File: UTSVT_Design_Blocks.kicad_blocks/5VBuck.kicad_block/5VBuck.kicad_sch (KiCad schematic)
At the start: 9 parts, among them U2 LMR51635XDDCR

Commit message: buck
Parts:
- removed C8: C_Small, symbol Device:C_Small
- C1: LCSC # C1607 -> (none); LCSC P/N (none) -> C1607; P/N (none) -> 581-0603YC225MAT2A
- C10, C9: footprint Capacitor_SMD:C_1210_3225Metric_Pad1.33x2.70mm_HandSolder -> Capacitor_SMD:C_0805_2012Metric_Pad1.18x1.45mm_HandSolder; LCSC P/N (none) -> C342635; P/N 81-GGM32ED70J476KE2L -> 581-TACR336K004X
- C2: footprint Capacitor_SMD:C_0603_1608Metric_Pad1.08x0.95mm_HandSolder -> Resistor_SMD:R_0201_0603Metric_Pad0.64x0.40mm_HandSolder; LCSC # C440198 -> (none); LCSC P/N (none) -> C14663
- L2: footprint Inductor_SMD:L_Sunlord_SWPA4020S -> Inductor_SMD:L_Cenker_CKCS252010; LCSC # C88247 -> (none); LCSC P/N (none) -> C354548; P/N (none) -> 810-VLS3015CX-100M-H
- R2: value 53.6 -> 53.6k; footprint Resistor_SMD:R_0603_1608Metric_Pad0.98x0.95mm_HandSolder -> Resistor_SMD:R_0201_0603Metric_Pad0.64x0.40mm_HandSolder; LCSC P/N (none) -> C23074; P/N 71-CRCW0603-53.6 -> 667-ERA-3ARB5362V; now fitted
- R3: footprint Capacitor_SMD:C_0402_1005Metric_Pad0.74x0.62mm_HandSolder -> Resistor_SMD:R_0201_0603Metric_Pad0.64x0.40mm_HandSolder; LCSC # C11660 -> (none); LCSC P/N (none) -> C22772; P/N (none) -> 603-RT0603DRE0710K2L; now fitted
- U2: LCSC P/N (none) -> C42432812; P/N (none) -> 595-LMR51635XDDCR
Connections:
- net V_in renamed V_in_24V
- net V_out renamed V_out_5V
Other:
- moved on the sheet: C10, C9, L2

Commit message: made changes
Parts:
- removed C10, C9: 33u, Capacitor_SMD:C_0805_2012Metric_Pad1.18x1.45mm_HandSolder, symbol Device:C_Small
- added C5, C8: 47u, Capacitor_SMD:C_1210_3225Metric_Pad1.33x2.70mm_HandSolder, symbol Device:C_Small
- C1: footprint Capacitor_SMD:C_0603_1608Metric_Pad1.08x0.95mm_HandSolder -> Capacitor_SMD:C_0805_2012Metric_Pad1.18x1.45mm_HandSolder; LCSC P/N C1607 -> C1771; P/N 581-0603YC225MAT2A -> 963-T21GCB7225MTPA1J
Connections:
- net GND: now also C5.2, C8.2
- net V_out_5V: now also C5.1, C8.1
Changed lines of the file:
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@@
 			)
 		)
-		(property "Footprint" "Capacitor_SMD:C_0603_1608Metric_Pad1.08x0.95mm_HandSolder"
+		(property "Footprint" "Capacitor_SMD:C_0805_2012Metric_Pad1.18x1.45mm_HandSolder"
 			(at 97.79 90.17 0)
 			(effects
@@
 			)
 		)
-		(property "LCSC P/N" "C1607"
+		(property "LCSC P/N" "C1771"
 			(at 97.79 90.17 0)
 			(effects
@@
 			)
 		)
-		(property "P/N" "581-0603YC225MAT2A"
+		(property "P/N" "963-T21GCB7225MTPA1J"
 			(at 97.79 90.17 0)
 			(effects
@@
 	)
 	(symbol
-		(lib_id "Device:C_Small")
-		(at 175.26 93.98 0)
-		(unit 1)
-		(exclude_from_sim no)
-		(in_bom yes)
-		(on_board yes)
-		(dnp no)
-		(fields_autoplaced yes)
-		(property "Reference" "C9"
-			(at 177.8 92.7162 0)
-			(effects
-				(font
-					(size 1.27 1.27)
-				)
-				(justify left)
-			)
-		)
-		(property "Value" "33u"
-			(at 177.8 95.2562 0)
-			(effects
-				(font
-					(size 1.27 1.27)
-				)
-				(justify left)
-			)
-		)
-		(property "Footprint" "Capacitor_SMD:C_0805_2012Metric_Pad1.18x1.45mm_HandSolder"
-			(at 175.26 93.98 0)
-			(effects
-				(font
-					(size 1.27 1.27)
-				)
-				(hide yes)
-			)
-		)
-		(property "Datasheet" "~"
-			(at 175.26 93.98 0)
-			(effects
-				(font
-					(size 1.27 1.27)
-				)
-				(hide yes)
-			)
-		)
-		(property "Description" "Unpolarized capacitor, small symbol"
-			(at 175.26 93.98 0)
-			(effects
-				(font
-					(size 1.27 1.27)
-				)
-				(hide yes)
-			)
-		)
-		(property "P/N" "581-TACR336K004X"
-			(at 175.26 93.98 0)
-			(effects
-				(font
-					(size 1.27 1.27)
-				)
-				(hide yes)
-			)
-		)
-		(property "LCSC P/N" "C342635"
-			(at 175.26 93.98 0)
-			(effects
-				(font
-					(size 1.27 1.27)
-				)
-				(hide yes)
-			)
-		)
-		(pin "1"
-		)
-		(pin "2"
-		)
-		(instances
-			(project "PS-Buck"
-				(path "/331f457b-ed4e-4d4a-ad6d-c8acb2febfed/fd0ad9ec-55a0-4daf-b550-9a7f2436753f"
-					(reference "C9")
-					(unit 1)
-				)
-			)
-		)
-	)
-	(symbol
 		(lib_id "power:PWR_FLAG")
 		(at 153.67 85.09 0)
@@
 				(path "/331f457b-ed4e-4d4a-ad6d-c8acb2febfed/fd0ad9ec-55a0-4daf-b550-9a7f2436753f"
 					(reference "#FLG08")
+					(unit 1)
+				)
+			)
+		)
+	)
+	(symbol
+		(lib_id "Device:C_Small")
+		(at 186.69 93.98 0)
+		(unit 1)
+		(exclude_from_sim no)
+		(in_bom yes)
+		(on_board yes)
+		(dnp no)
+		(fields_autoplaced yes)
+		(property "Reference" "C8"
+			(at 189.23 92.7162 0)
+			(effects
+				(font
+					(size 1.27 1.27)
+				)
+				(justify left)
+			)
+		)
+		(property "Value" "47u"
+			(at 189.23 95.2562 0)
+			(effects
+				(font
+					(size 1.27 1.27)
+				)
+				(justify left)
+			)
+		)
+		(property "Footprint" "Capacitor_SMD:C_1210_3225Metric_Pad1.33x2.70mm_HandSolder"
+			(at 186.69 93.98 0)
+			(effects
+				(font
+					(size 1.27 1.27)
+				)
+				(hide yes)
+			)
+		)
+		(property "Datasheet" "~"
+			(at 186.69 93.98 0)
+			(effects
+				(font
+					(size 1.27 1.27)
+				)
+				(hide yes)
+			)
+		)
+		(property "Description" "Unpolarized capacitor, small symbol"
+			(at 186.69 93.98 0)
+			(effects
+				(font
+					(size 1.27 1.27)
+				)
+				(hide yes)
+			)
+		)
+		(property "P/N" "963-MLAST32MAB5476MP"
+			(at 186.69 93.98 0)
+			(effects
+				(font
+					(size 1.27 1.27)
+				)
+				(hide yes)
+			)
+		)
+		(property "LCSC P/N" "C77101"
+			(at 186.69 93.98 0)
+			(effects
+				(font
+					(size 1.27 1.27)
+				)
+				(hide yes)
+			)
+		)
+		(pin "1"
+		)
+		(pin "2"
+		)
+		(instances
+			(project "PS-Buck"
+				(path "/331f457b-ed4e-4d4a-ad6d-c8acb2febfed/fd0ad9ec-55a0-4daf-b550-9a7f2436753f"
+					(reference "C8")
 					(unit 1)
 				)
@@
 	(symbol
 		(lib_id "Device:C_Small")
-		(at 186.69 93.98 0)
+		(at 175.26 93.98 0)
 		(unit 1)
 		(exclude_from_sim no)
@@
 		(dnp no)
 		(fields_autoplaced yes)
-		(property "Reference" "C10"
-			(at 189.23 92.7162 0)
-			(effects
-				(font
-					(size 1.27 1.27)
-				)
-				(justify left)
-			)
-		)
-		(property "Value" "33u"
-			(at 189.23 95.2562 0)
-			(effects
-				(font
-					(size 1.27 1.27)
-				)
-				(justify left)
-			)
-		)
-		(property "Footprint" "Capacitor_SMD:C_0805_2012Metric_Pad1.18x1.45mm_HandSolder"
-			(at 186.69 93.98 0)
+		(property "Reference" "C5"
+			(at 177.8 92.7162 0)
+			(effects
+				(font
+					(size 1.27 1.27)
+				)
+				(justify left)
+			)
+		)
+		(property "Value" "47u"
+			(at 177.8 95.2562 0)
+			(effects
+				(font
+					(size 1.27 1.27)
+				)
+				(justify left)
+			)
+		)
+		(property "Footprint" "Capacitor_SMD:C_1210_3225Metric_Pad1.33x2.70mm_HandSolder"
+			(at 175.26 93.98 0)
 			(effects
 				(font
@@
 		)
 		(property "Datasheet" "~"
-			(at 186.69 93.98 0)
+			(at 175.26 93.98 0)
 			(effects
 				(font
@@
 		)
 		(property "Description" "Unpolarized capacitor, small symbol"
-			(at 186.69 93.98 0)
-			(effects
-				(font
-					(size 1.27 1.27)
-				)
-				(hide yes)
-			)
-		)
-		(property "P/N" "581-TACR336K004X"
-			(at 186.69 93.98 0)
-			(effects
-				(font
-					(size 1.27 1.27)
-				)
-				(hide yes)
-			)
-		)
-		(property "LCSC P/N" "C342635"
-			(at 186.69 93.98 0)
+			(at 175.26 93.98 0)
+			(effects
+				(font
+					(size 1.27 1.27)
+				)
+				(hide yes)
+			)
+		)
+		(property "P/N" "963-MLAST32MAB5476MP"
+			(at 175.26 93.98 0)
+			(effects
+				(font
+					(size 1.27 1.27)
+				)
+				(hide yes)
+			)
+		)
+		(property "LCSC P/N" "C77101"
+			(at 175.26 93.98 0)
 			(effects
 				(font
@@
 			(project "PS-Buck"
 				(path "/331f457b-ed4e-4d4a-ad6d-c8acb2febfed/fd0ad9ec-55a0-4daf-b550-9a7f2436753f"
-					(reference "C10")
-					(unit 1)
-				)
+					(reference "C5")
+					(unit 1)
+				)

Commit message: review addressed
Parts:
- C1: P/N 963-T21GCB7225MTPA1J -> CL21F225ZAFNNNE
- C5, C8: P/N 963-MLAST32MAB5476MP -> GRM32ER61C476KE15L
- L2: footprint Inductor_SMD:L_Cenker_CKCS252010 -> Inductor_SMD:L_TDK_VLP8040; LCSC P/N C354548 -> C354639; P/N 810-VLS3015CX-100M-H -> CKCS8040-10uH/M
- R2: P/N 667-ERA-3ARB5362V -> 0603WAF5362T5E
- R3: P/N 603-RT0603DRE0710K2L -> 0603WAF1022T5E
- U2: footprint breh:DDC0006A-MFG -> utsvt_ics:DDC0006A-MFG; P/N 595-LMR51635XDDCR -> LMR51635XDDCR
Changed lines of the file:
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@@
 			)
 		)
-		(property "Footprint" "Inductor_SMD:L_Cenker_CKCS252010"
+		(property "Footprint" "Inductor_SMD:L_TDK_VLP8040"
 			(at 166.37 90.17 0)
 			(effects
@@
 			)
 		)
-		(property "LCSC P/N" "C354548"
+		(property "LCSC P/N" "C354639"
 			(at 166.37 90.17 90)
 			(effects
@@
 			)
 		)
-		(property "P/N" "810-VLS3015CX-100M-H"
+		(property "P/N" "CKCS8040-10uH/M"
 			(at 166.37 90.17 90)
 			(effects
@@
 			)
 		)
-		(property "P/N" "603-RT0603DRE0710K2L"
+		(property "P/N" "0603WAF1022T5E"
 			(at 227.33 93.98 0)
 			(effects
@@
 			)
 		)
-		(property "P/N" "963-T21GCB7225MTPA1J"
+		(property "P/N" "CL21F225ZAFNNNE"
 			(at 97.79 90.17 0)
 			(effects
@@
 			)
 		)
-		(property "Footprint" "breh:DDC0006A-MFG"
+		(property "Footprint" "utsvt_ics:DDC0006A-MFG"
 			(at 118.11 85.09 0)
 			(effects
@@
 			)
 		)
-		(property "P/N" "595-LMR51635XDDCR"
+		(property "P/N" "LMR51635XDDCR"
 			(at 118.11 85.09 0)
 			(effects
@@
 			)
 		)
-		(property "P/N" "963-MLAST32MAB5476MP"
+		(property "P/N" "GRM32ER61C476KE15L"
 			(at 186.69 93.98 0)
 			(effects
@@
 			)
 		)
-		(property "P/N" "667-ERA-3ARB5362V"
+		(property "P/N" "0603WAF5362T5E"
 			(at 227.33 86.36 0)
 			(effects
@@
 			)
 		)
-		(property "P/N" "963-MLAST32MAB5476MP"
+		(property "P/N" "GRM32ER61C476KE15L"
 			(at 175.26 93.98 0)
 			(effects

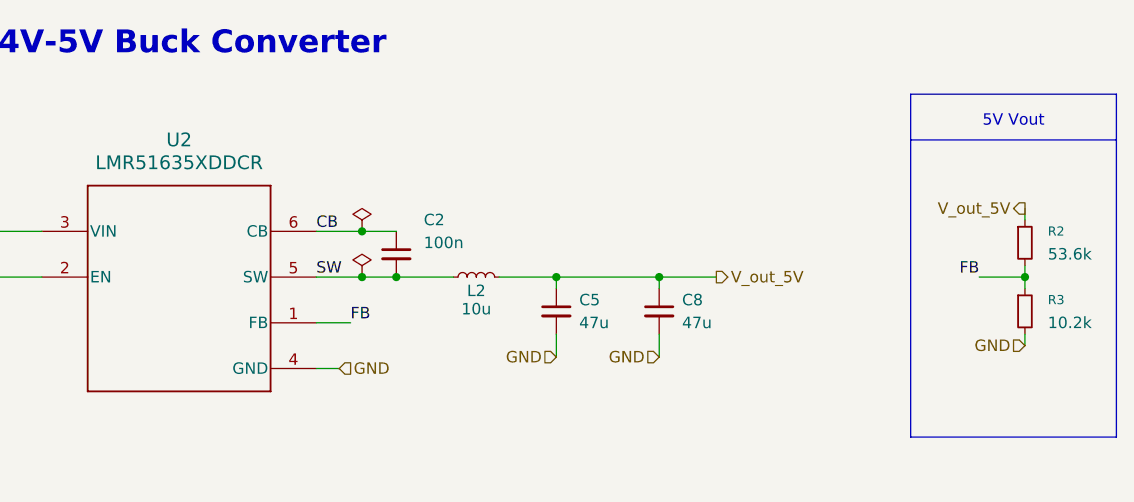
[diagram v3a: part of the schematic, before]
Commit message: fixed designators
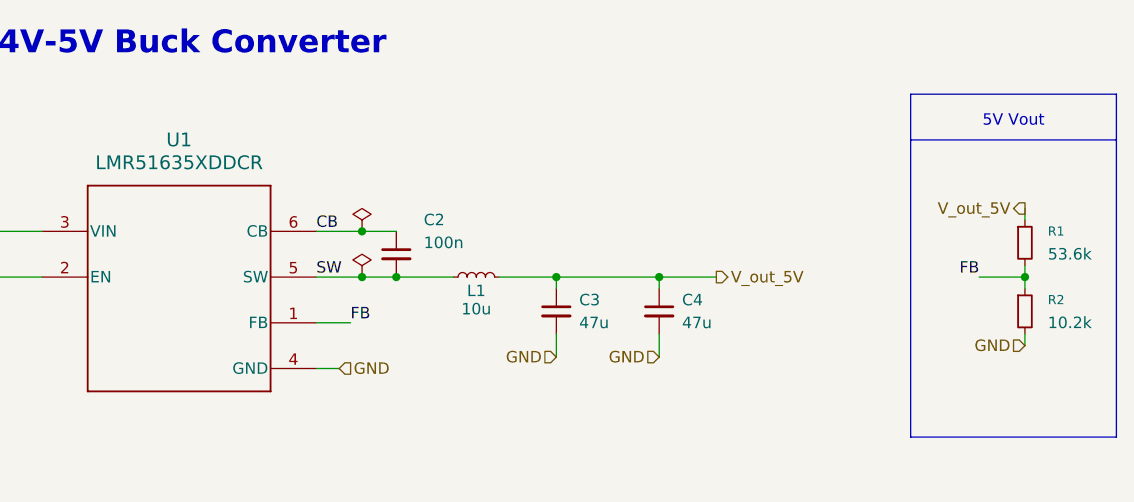
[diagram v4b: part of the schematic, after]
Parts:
- renumbered C5 to C3, C8 to C4, L2 to L1, R2 to R1, R3 to R2, U2 to U1
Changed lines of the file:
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@@
 		(on_board yes)
 		(dnp no)
-		(property "Reference" "L2"
+		(property "Reference" "L1"
 			(at 166.37 91.694 90)
 			(effects
@@
 		)
 		(instances
+			(project "5VBuck"
+				(path "/1a7db697-3478-4f8f-a838-af5608c43196"
+					(reference "L1")
+					(unit 1)
+				)
+			)
 			(project "PS-Buck"
 				(path "/331f457b-ed4e-4d4a-ad6d-c8acb2febfed/fd0ad9ec-55a0-4daf-b550-9a7f2436753f"
@@
 		(dnp no)
 		(fields_autoplaced yes)
-		(property "Reference" "R3"
+		(property "Reference" "R2"
 			(at 229.87 92.7099 0)
 			(effects
@@
 		)
 		(instances
+			(project "5VBuck"
+				(path "/1a7db697-3478-4f8f-a838-af5608c43196"
+					(reference "R2")
+					(unit 1)
+				)
+			)
 			(project "PS-Buck"
 				(path "/331f457b-ed4e-4d4a-ad6d-c8acb2febfed/fd0ad9ec-55a0-4daf-b550-9a7f2436753f"
@@
 		)
 		(instances
+			(project "5VBuck"
+				(path "/1a7db697-3478-4f8f-a838-af5608c43196"
+					(reference "C1")
+					(unit 1)
+				)
+			)
 			(project "PS-Buck"
 				(path "/331f457b-ed4e-4d4a-ad6d-c8acb2febfed/fd0ad9ec-55a0-4daf-b550-9a7f2436753f"
@@
 		)
 		(instances
+			(project "5VBuck"
+				(path "/1a7db697-3478-4f8f-a838-af5608c43196"
+					(reference "C2")
+					(unit 1)
+				)
+			)
 			(project "PS-Buck"
 				(path "/331f457b-ed4e-4d4a-ad6d-c8acb2febfed/fd0ad9ec-55a0-4daf-b550-9a7f2436753f"
@@
 		(dnp no)
 		(fields_autoplaced yes)
-		(property "Reference" "U2"
+		(property "Reference" "U1"
 			(at 133.35 74.93 0)
 			(effects
@@
 		)
 		(instances
+			(project "5VBuck"
+				(path "/1a7db697-3478-4f8f-a838-af5608c43196"
+					(reference "U1")
+					(unit 1)
+				)
+			)
 			(project "PS-Buck"
 				(path "/331f457b-ed4e-4d4a-ad6d-c8acb2febfed/fd0ad9ec-55a0-4daf-b550-9a7f2436753f"
@@
 		(dnp no)
 		(fields_autoplaced yes)
-		(property "Reference" "#FLG08"
+		(property "Reference" "#FLG01"
 			(at 153.67 83.185 0)
 			(effects
@@
 		)
 		(instances
+			(project "5VBuck"
+				(path "/1a7db697-3478-4f8f-a838-af5608c43196"
+					(reference "#FLG01")
+					(unit 1)
+				)
+			)
 			(project "PS-Buck"
 				(path "/331f457b-ed4e-4d4a-ad6d-c8acb2febfed/fd0ad9ec-55a0-4daf-b550-9a7f2436753f"
@@
 		(dnp no)
 		(fields_autoplaced yes)
-		(property "Reference" "C8"
+		(property "Reference" "C4"
 			(at 189.23 92.7162 0)
 			(effects
@@
 		)
 		(instances
+			(project "5VBuck"
+				(path "/1a7db697-3478-4f8f-a838-af5608c43196"
+					(reference "C4")
+					(unit 1)
+				)
+			)
 			(project "PS-Buck"
 				(path "/331f457b-ed4e-4d4a-ad6d-c8acb2febfed/fd0ad9ec-55a0-4daf-b550-9a7f2436753f"
@@
 		(on_board yes)
 		(dnp no)
-		(property "Reference" "#FLG09"
+		(property "Reference" "#FLG02"
 			(at 153.67 88.265 0)
 			(effects
@@
 		)
 		(instances
+			(project "5VBuck"
+				(path "/1a7db697-3478-4f8f-a838-af5608c43196"
+					(reference "#FLG02")
+					(unit 1)
+				)
+			)
 			(project "PS-Buck"
 				(path "/331f457b-ed4e-4d4a-ad6d-c8acb2febfed/fd0ad9ec-55a0-4daf-b550-9a7f2436753f"
@@
 		(dnp no)
 		(fields_autoplaced yes)
-		(property "Reference" "R2"
+		(property "Reference" "R1"
 			(at 229.87 85.0899 0)
 			(effects
@@
 		)
 		(instances
+			(project "5VBuck"
+				(path "/1a7db697-3478-4f8f-a838-af5608c43196"
+					(reference "R1")
+					(unit 1)
+				)
+			)
 			(project "PS-Buck"
 				(path "/331f457b-ed4e-4d4a-ad6d-c8acb2febfed/fd0ad9ec-55a0-4daf-b550-9a7f2436753f"
@@
 		(dnp no)
 		(fields_autoplaced yes)
-		(property "Reference" "C5"
+		(property "Reference" "C3"
 			(at 177.8 92.7162 0)
 			(effects
@@
 		)
 		(instances
+			(project "5VBuck"
+				(path "/1a7db697-3478-4f8f-a838-af5608c43196"
+					(reference "C3")
+					(unit 1)
+				)
+			)
 			(project "PS-Buck"
 				(path "/331f457b-ed4e-4d4a-ad6d-c8acb2febfed/fd0ad9ec-55a0-4daf-b550-9a7f2436753f"
@@
 		)
 	)
+	(sheet_instances
+		(path "/"
+			(page "1")
+		)
+	)
+	(embedded_fonts no)
 )

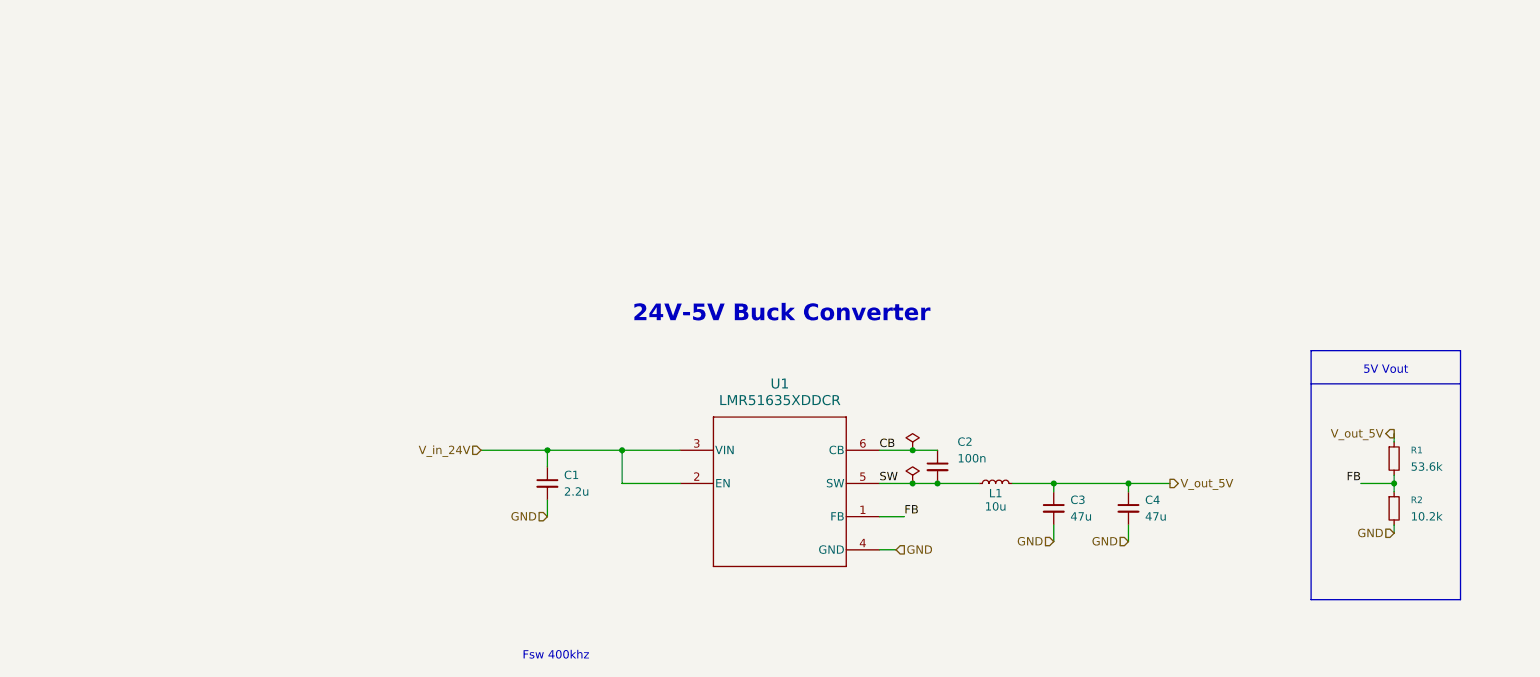
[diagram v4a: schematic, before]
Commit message: added test points to 5V buck to merge
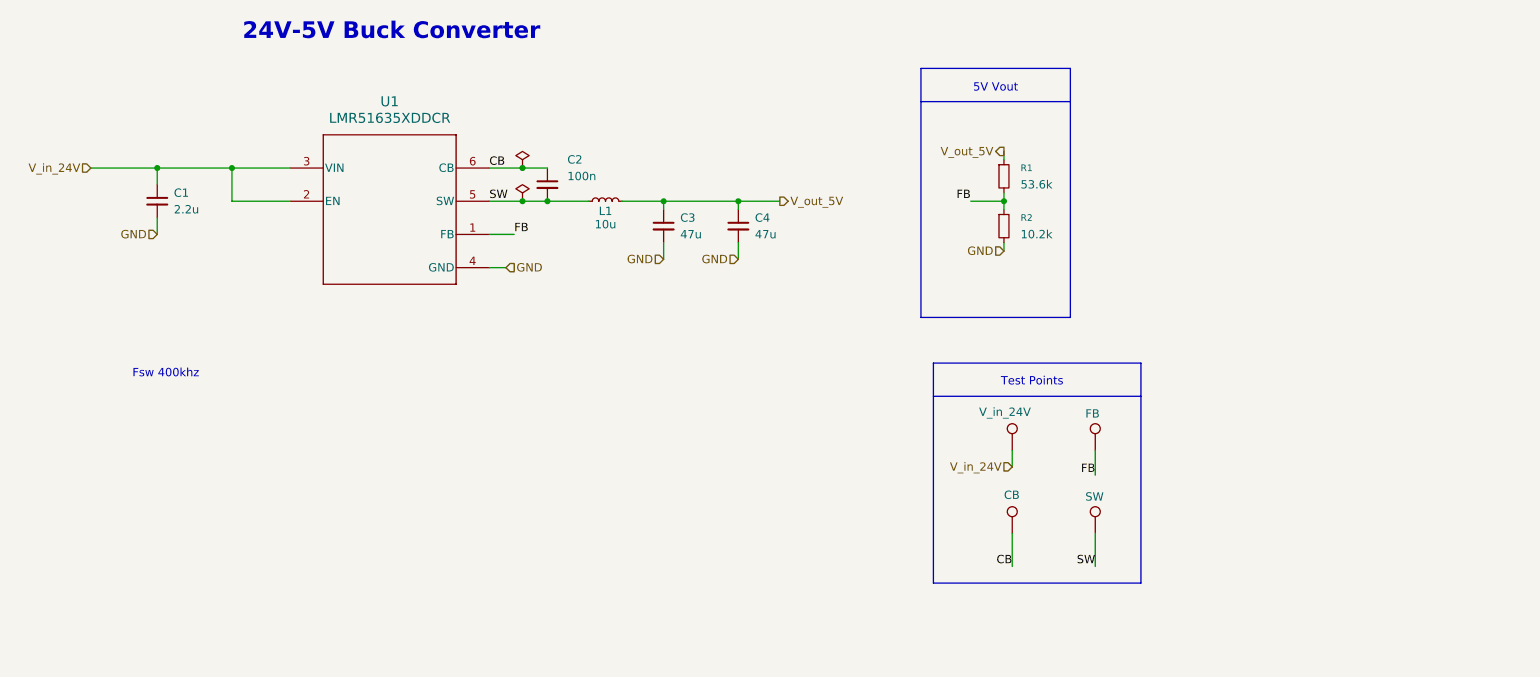
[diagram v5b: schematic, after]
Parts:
- added TP5: V_in_24V, symbol Connector:TestPoint
- added TP6: FB, symbol Connector:TestPoint
- added TP7: CB, symbol Connector:TestPoint
- added TP8: SW, symbol Connector:TestPoint
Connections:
- net CB: now also TP7.1
- net FB: now also TP6.1
- net SW: now also TP8.1
- net V_in_24V: now also TP5.1
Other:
- note added: "Test Points"
- moved on the sheet: C1, C2, C3, C4, L1, R1, R2, U1
